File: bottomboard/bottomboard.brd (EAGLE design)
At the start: 13 x 75 mm, 16 parts, among them P1 PAD, P2 PAD, P3 PAD, P4 PAD, Q1 SIA436DJ, U1 AP7215-33YG-13

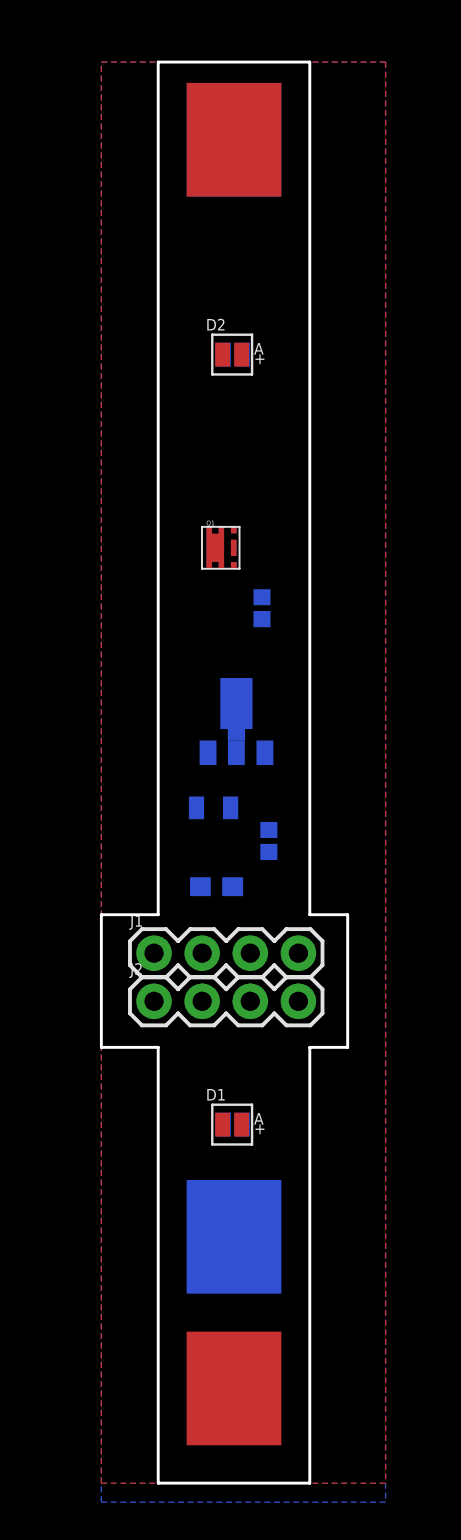
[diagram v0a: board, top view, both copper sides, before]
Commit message: Initial bottom board design done
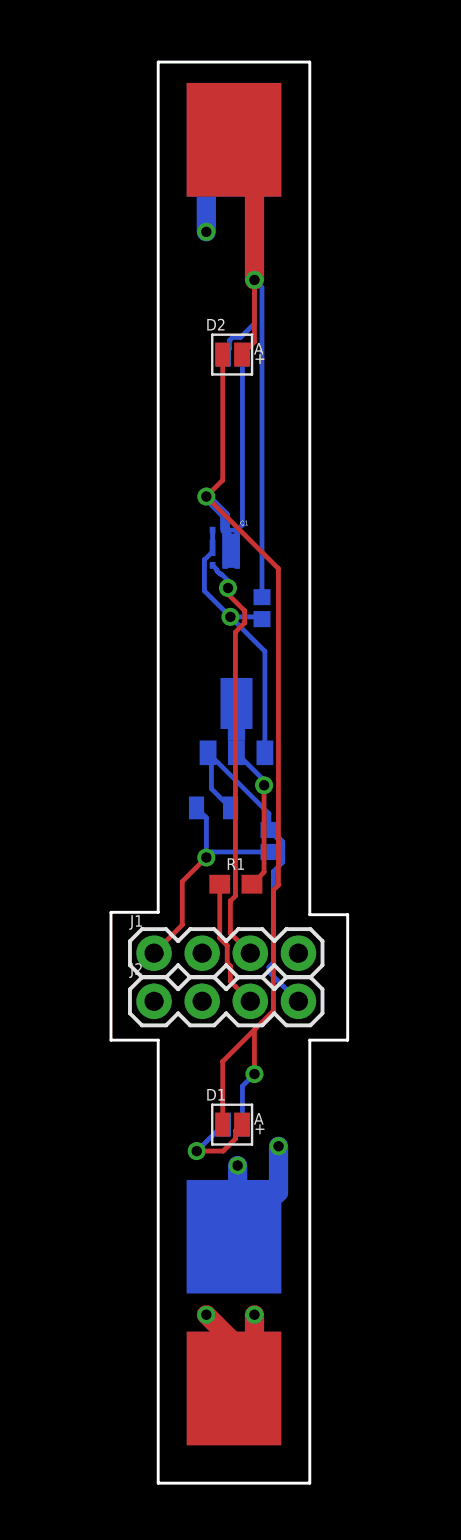
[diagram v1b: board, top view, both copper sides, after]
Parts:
- moved Q1 1.78 mm to (4.32, 48.3), flipped to the bottom
- moved R1 1.02 mm to (4.10, 31.6), flipped to the top
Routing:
- net N$2: track 0.00 -> 64.5 mm, vias 0 -> 2
- net VCC: track 0.00 -> 55.7 mm, vias 0 -> 5
- net GND: track 0.00 -> 42.2 mm, vias 0 -> 5
- net GPIO-0: track 0.00 -> 22.0 mm, vias 0 -> 1
- net 3.3V: track 0.00 -> 19.2 mm
- net RESET: track 0.00 -> 6.85 mm
- added copper zone on layer 15, net GND
- added copper zone on layer 2, net VCC
- removed copper zone on layer 16, net GND
- removed copper zone on layer 1, net VCC
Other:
- board size 13 x 75 mm -> 12.5 x 75 mm

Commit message: Started on middle board
Need to figure out how to daisy chain transistors.
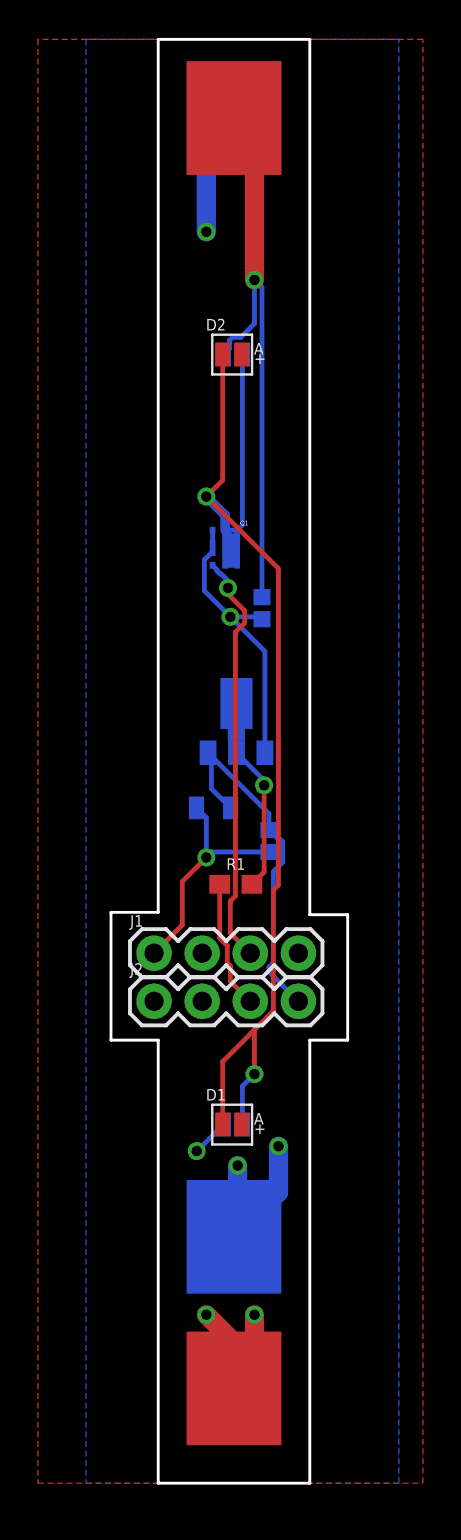
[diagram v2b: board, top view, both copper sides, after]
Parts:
- moved P3 1.14 mm to (4.00, 72.0)
- moved P4 1.14 mm to (4.00, 72.0)
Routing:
- net VCC: track 55.7 -> 49.4 mm
- net GND: track 42.2 -> 43.3 mm
- added copper zone on layer 16, net GND
- added copper zone on layer 1, net VCC
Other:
- board size 12.5 x 75 mm -> 12.5 x 76.2 mm
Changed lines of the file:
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@@
 <plain>
 <wire x1="0" y1="0" x2="0" y2="23.381" width="0.1524" layer="20"/>
-<wire x1="0" y1="30.127" x2="0" y2="75" width="0.1524" layer="20"/>
-<wire x1="0" y1="75" x2="8" y2="75" width="0.1524" layer="20"/>
-<wire x1="8" y1="75" x2="8" y2="30" width="0.1524" layer="20"/>
+<wire x1="0" y1="30.127" x2="0" y2="76.2" width="0.1524" layer="20"/>
+<wire x1="0" y1="76.2" x2="8" y2="76.2" width="0.1524" layer="20"/>
+<wire x1="8" y1="76.2" x2="8" y2="30" width="0.1524" layer="20"/>
 <wire x1="8" y1="23.381" x2="8" y2="0" width="0.1524" layer="20"/>
 <wire x1="8" y1="0" x2="0" y2="0" width="0.1524" layer="20"/>
@@
 <element name="P1" library="pad" package="PAD" value="PAD" x="4" y="5" smashed="yes"/>
 <element name="P2" library="pad" package="PAD" value="PAD" x="4" y="13" smashed="yes" rot="MR0"/>
-<element name="P3" library="pad" package="PAD" value="PAD" x="4" y="70.9" smashed="yes"/>
-<element name="P4" library="pad" package="PAD" value="PAD" x="4" y="70.9" smashed="yes" rot="MR0"/>
+<element name="P3" library="pad" package="PAD" value="PAD" x="4" y="72.043" smashed="yes"/>
+<element name="P4" library="pad" package="PAD" value="PAD" x="4" y="72.043" smashed="yes" rot="MR0"/>
 </elements>
 <signals>
@@
 <wire x1="4.946" y1="31.607" x2="5.588" y2="32.249" width="0.254" layer="1"/>
 <wire x1="5.588" y1="32.249" x2="5.588" y2="36.83" width="0.254" layer="1"/>
-<wire x1="4.404359375" y1="18.923" x2="4.08305" y2="18.601690625" width="0.254" layer="1"/>
-<wire x1="4.08305" y1="18.601690625" x2="4.08305" y2="18.17735" width="0.254" layer="1"/>
-<wire x1="4.08305" y1="18.17735" x2="3.4317" y2="17.526" width="0.254" layer="1"/>
-<wire x1="3.4317" y1="17.526" x2="2.032" y2="17.526" width="0.254" layer="1"/>
 <via x="5.08" y="63.5" extent="1-16" drill="0.55"/>
-<wire x1="4.404359375" y1="59.563" x2="5.08" y2="60.238640625" width="0.254" layer="1"/>
-<wire x1="5.08" y1="60.238640625" x2="5.08" y2="63.5" width="0.254" layer="1"/>
+<wire x1="5.08" y1="63.5" x2="5.08" y2="70.963" width="1.016" layer="1"/>
+<wire x1="5.08" y1="70.963" x2="4" y2="72.043" width="1.016" layer="1"/>
+<polygon width="0.254" layer="1">
+<vertex x="-6.35" y="0"/>
+<vertex x="13.97" y="0"/>
+<vertex x="13.97" y="76.2"/>
+<vertex x="-6.35" y="76.2"/>
+</polygon>
 <wire x1="5.08" y1="61.198759375" x2="5.08" y2="63.5" width="0.254" layer="16"/>
+<wire x1="3.444240625" y1="59.563" x2="3.76555" y2="59.884309375" width="0.254" layer="16"/>
+<wire x1="3.76555" y1="59.884309375" x2="3.76555" y2="60.30865" width="0.254" layer="16"/>
+<wire x1="3.76555" y1="60.30865" x2="3.92921875" y2="60.47231875" width="0.254" layer="16"/>
 <wire x1="3.92921875" y1="60.47231875" x2="4.353559375" y2="60.47231875" width="0.254" layer="16"/>
 <wire x1="4.353559375" y1="60.47231875" x2="5.08" y2="61.198759375" width="0.254" layer="16"/>
-<wire x1="3.7592" y1="59.877959375" x2="3.7592" y2="60.3023" width="0.254" layer="16"/>
-<wire x1="3.7592" y1="60.3023" x2="3.92921875" y2="60.47231875" width="0.254" layer="16"/>
 <wire x1="5.477" y1="46.76" x2="5.477" y2="63.103" width="0.254" layer="16"/>
 <wire x1="5.477" y1="63.103" x2="5.08" y2="63.5" width="0.254" layer="16"/>
-<wire x1="5.08" y1="63.5" x2="5.08" y2="69.82" width="1.016" layer="1"/>
-<wire x1="5.08" y1="69.82" x2="4" y2="70.9" width="1.016" layer="1"/>
-<wire x1="3.444240625" y1="59.563" x2="3.7592" y2="59.877959375" width="0.254" layer="16"/>
 </signal>
 <signal name="N$2">
@@
 <wire x1="1.27" y1="29.46" x2="1.27" y2="31.75" width="0.254" layer="1"/>
 <via x="2.54" y="66.04" extent="1-16" drill="0.55"/>
-<wire x1="2.54" y1="66.04" x2="2.54" y2="69.44" width="1.016" layer="16"/>
-<wire x1="2.54" y1="69.44" x2="4" y2="70.9" width="1.016" layer="16"/>
+<wire x1="2.54" y1="66.04" x2="2.54" y2="70.583" width="1.016" layer="16"/>
+<wire x1="2.54" y1="70.583" x2="4" y2="72.043" width="1.016" layer="16"/>
+<polygon width="0.254" layer="16">
+<vertex x="-3.81" y="0"/>
+<vertex x="12.7" y="0"/>
+<vertex x="12.7" y="76.2"/>
+<vertex x="-3.81" y="76.2"/>
+</polygon>
 </signal>
 <signal name="RX">

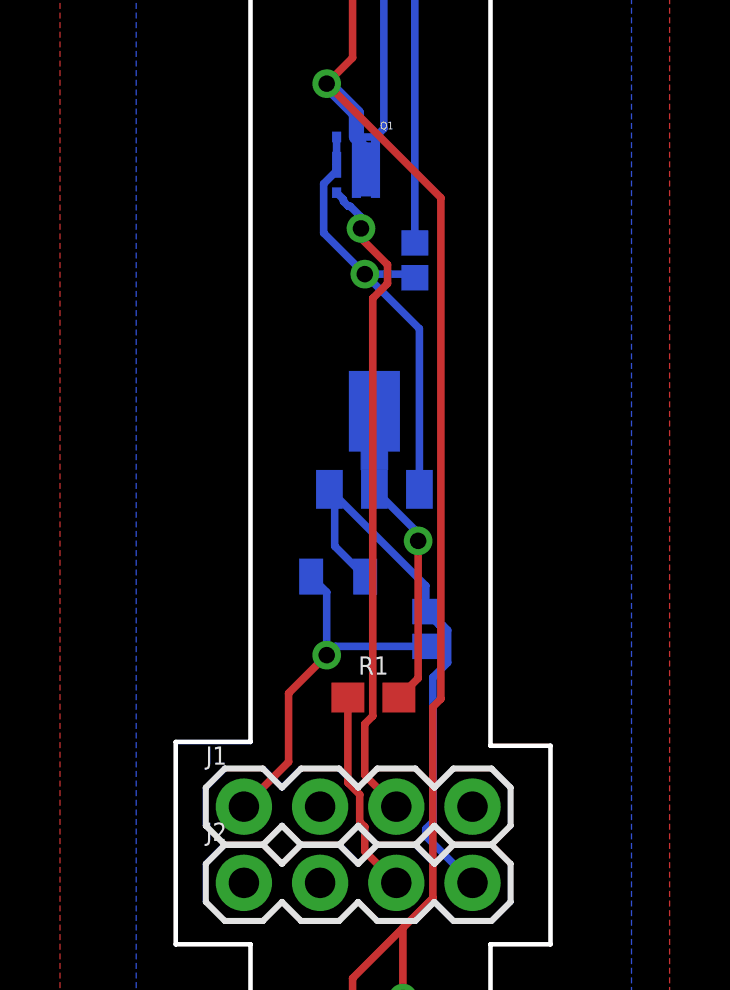
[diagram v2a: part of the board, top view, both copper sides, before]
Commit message: Increased via sizes
Increased via sizes in bottom and
middle boards so we can solder wires in them.
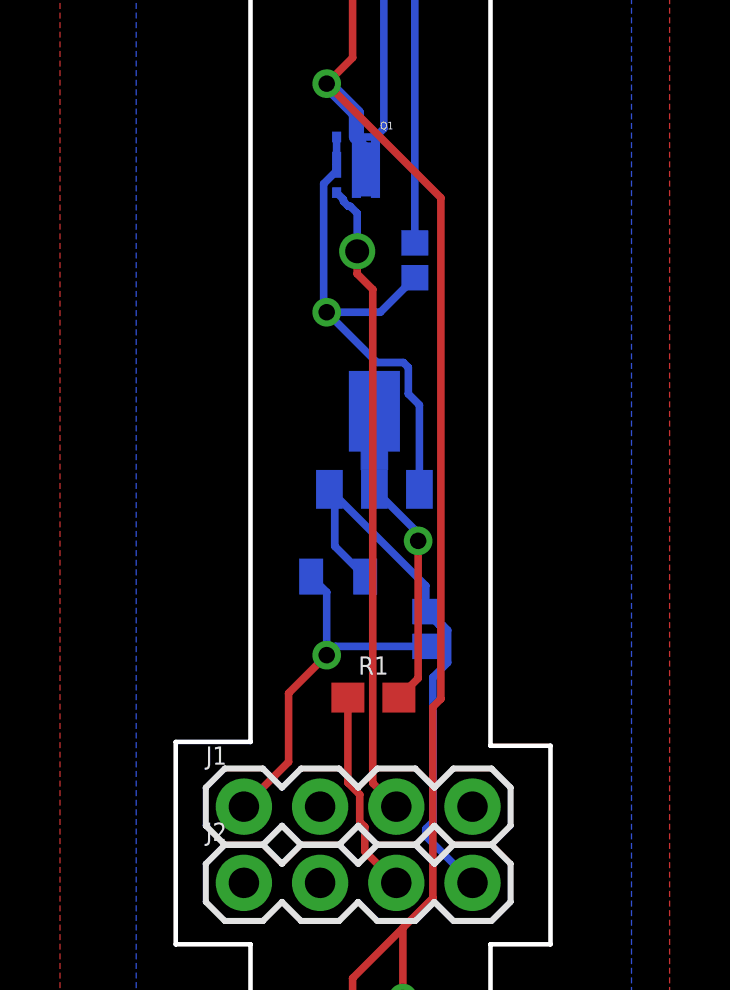
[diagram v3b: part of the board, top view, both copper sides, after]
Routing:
- net GND: track 43.3 -> 45.6 mm
- net GPIO-0: track 22.0 -> 21.3 mm
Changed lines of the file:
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@@
 <wire x1="4.191" y1="16.764" x2="4.191" y2="13.39" width="1.016" layer="16"/>
 <wire x1="4.191" y1="13.39" x2="4.39" y2="13.39" width="1.016" layer="16"/>
-<via x="3.81" y="45.72" extent="1-16" drill="0.55"/>
-<wire x1="5.477" y1="45.6" x2="5.357" y2="45.72" width="0.254" layer="16"/>
-<wire x1="5.357" y1="45.72" x2="3.81" y2="45.72" width="0.254" layer="16"/>
+<via x="2.54" y="44.45" extent="1-16" drill="0.55"/>
+<wire x1="5.477" y1="45.6" x2="4.327" y2="44.45" width="0.254" layer="16"/>
+<wire x1="4.327" y1="44.45" x2="2.54" y2="44.45" width="0.254" layer="16"/>
 <wire x1="2.8702" y1="49.3649" x2="2.8702" y2="50.292" width="0.254" layer="16"/>
 <wire x1="2.8702" y1="49.3649" x2="2.8702" y2="49.16313125" width="0.254" layer="16"/>
 <wire x1="2.8702" y1="49.16313125" x2="2.4384" y2="48.73133125" width="0.254" layer="16"/>
-<wire x1="2.4384" y1="47.0916" x2="3.81" y2="45.72" width="0.254" layer="16"/>
-<wire x1="2.4384" y1="48.73133125" x2="2.4384" y2="47.0916" width="0.254" layer="16"/>
+<wire x1="2.4384" y1="44.5516" x2="2.54" y2="44.45" width="0.254" layer="16"/>
+<wire x1="2.4384" y1="48.73133125" x2="2.4384" y2="44.5516" width="0.254" layer="16"/>
 <via x="2.54" y="33.02" extent="1-16" drill="0.55"/>
 <wire x1="2.021" y1="35.639" x2="2.54" y2="35.12" width="0.254" layer="16"/>
 <wire x1="2.54" y1="35.12" x2="2.54" y2="33.02" width="0.254" layer="16"/>
-<wire x1="5.63" y1="38.5458" x2="5.63" y2="43.9" width="0.254" layer="16"/>
-<wire x1="5.63" y1="43.9" x2="3.81" y2="45.72" width="0.254" layer="16"/>
+<wire x1="5.63" y1="38.5458" x2="5.63" y2="41.36" width="0.254" layer="16"/>
 <wire x1="5.842" y1="33.313" x2="2.833" y2="33.313" width="0.254" layer="16"/>
 <wire x1="2.833" y1="33.313" x2="2.54" y2="33.02" width="0.254" layer="16"/>
@@
 <vertex x="-3.81" y="76.2"/>
 </polygon>
+<wire x1="5.63" y1="41.36" x2="5.2603" y2="41.7297" width="0.254" layer="16"/>
+<wire x1="5.2603" y1="41.7297" x2="5.2603" y2="42.61123125" width="0.254" layer="16"/>
+<wire x1="5.2603" y1="42.61123125" x2="5.09663125" y2="42.7749" width="0.254" layer="16"/>
+<wire x1="5.09663125" y1="42.7749" x2="4.2151" y2="42.7749" width="0.254" layer="16"/>
+<wire x1="4.2151" y1="42.7749" x2="2.54" y2="44.45" width="0.254" layer="16"/>
 </signal>
 <signal name="RX">
@@
 <contactref element="J1" pad="3"/>
 <contactref element="Q1" pad="P$4"/>
-<wire x1="3.683" y1="47.625" x2="3.683" y2="47.244" width="0.254" layer="16"/>
-<via x="3.683" y="47.244" extent="1-16" drill="0.55"/>
+<wire x1="3.556" y1="47.752" x2="3.556" y2="46.482" width="0.254" layer="16"/>
+<via x="3.556" y="46.482" extent="1-16" drill="0.8"/>
 <wire x1="2.8702" y1="48.4378" x2="3.0988" y2="48.2092" width="0.254" layer="16"/>
 <wire x1="3.0988" y1="48.2092" x2="3.0988" y2="48.14426875" width="0.254" layer="16"/>
 <wire x1="3.0988" y1="48.14426875" x2="3.26246875" y2="47.9806" width="0.254" layer="16"/>
 <wire x1="3.26246875" y1="47.9806" x2="3.3274" y2="47.9806" width="0.254" layer="16"/>
-<wire x1="3.3274" y1="47.9806" x2="3.683" y2="47.625" width="0.254" layer="16"/>
-<wire x1="3.81" y1="29.02" x2="4.86" y2="27.97" width="0.254" layer="1"/>
-<wire x1="4.5676" y1="46.0338125" x2="4.5676" y2="45.4061875" width="0.254" layer="1"/>
-<wire x1="3.683" y1="47.244" x2="3.683" y2="46.9184125" width="0.254" layer="1"/>
-<wire x1="3.81" y1="30.72586875" x2="3.81" y2="29.02" width="0.254" layer="1"/>
-<wire x1="3.683" y1="46.9184125" x2="4.5676" y2="46.0338125" width="0.254" layer="1"/>
-<wire x1="4.0754" y1="30.99126875" x2="3.81" y2="30.72586875" width="0.254" layer="1"/>
-<wire x1="4.5676" y1="45.4061875" x2="4.0754" y2="44.9139875" width="0.254" layer="1"/>
-<wire x1="4.0754" y1="44.9139875" x2="4.0754" y2="30.99126875" width="0.254" layer="1"/>
+<wire x1="3.3274" y1="47.9806" x2="3.556" y2="47.752" width="0.254" layer="16"/>
+<wire x1="4.0754" y1="28.7546" x2="4.86" y2="27.97" width="0.254" layer="1"/>
+<wire x1="4.0754" y1="45.212" x2="4.0754" y2="28.7546" width="0.254" layer="1"/>
+<wire x1="3.556" y1="46.482" x2="3.556" y2="45.7314" width="0.254" layer="1"/>
+<wire x1="3.556" y1="45.7314" x2="4.0754" y2="45.212" width="0.254" layer="1"/>
 </signal>
 <signal name="GPIO-2">
